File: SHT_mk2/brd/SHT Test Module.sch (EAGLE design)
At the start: 12 parts

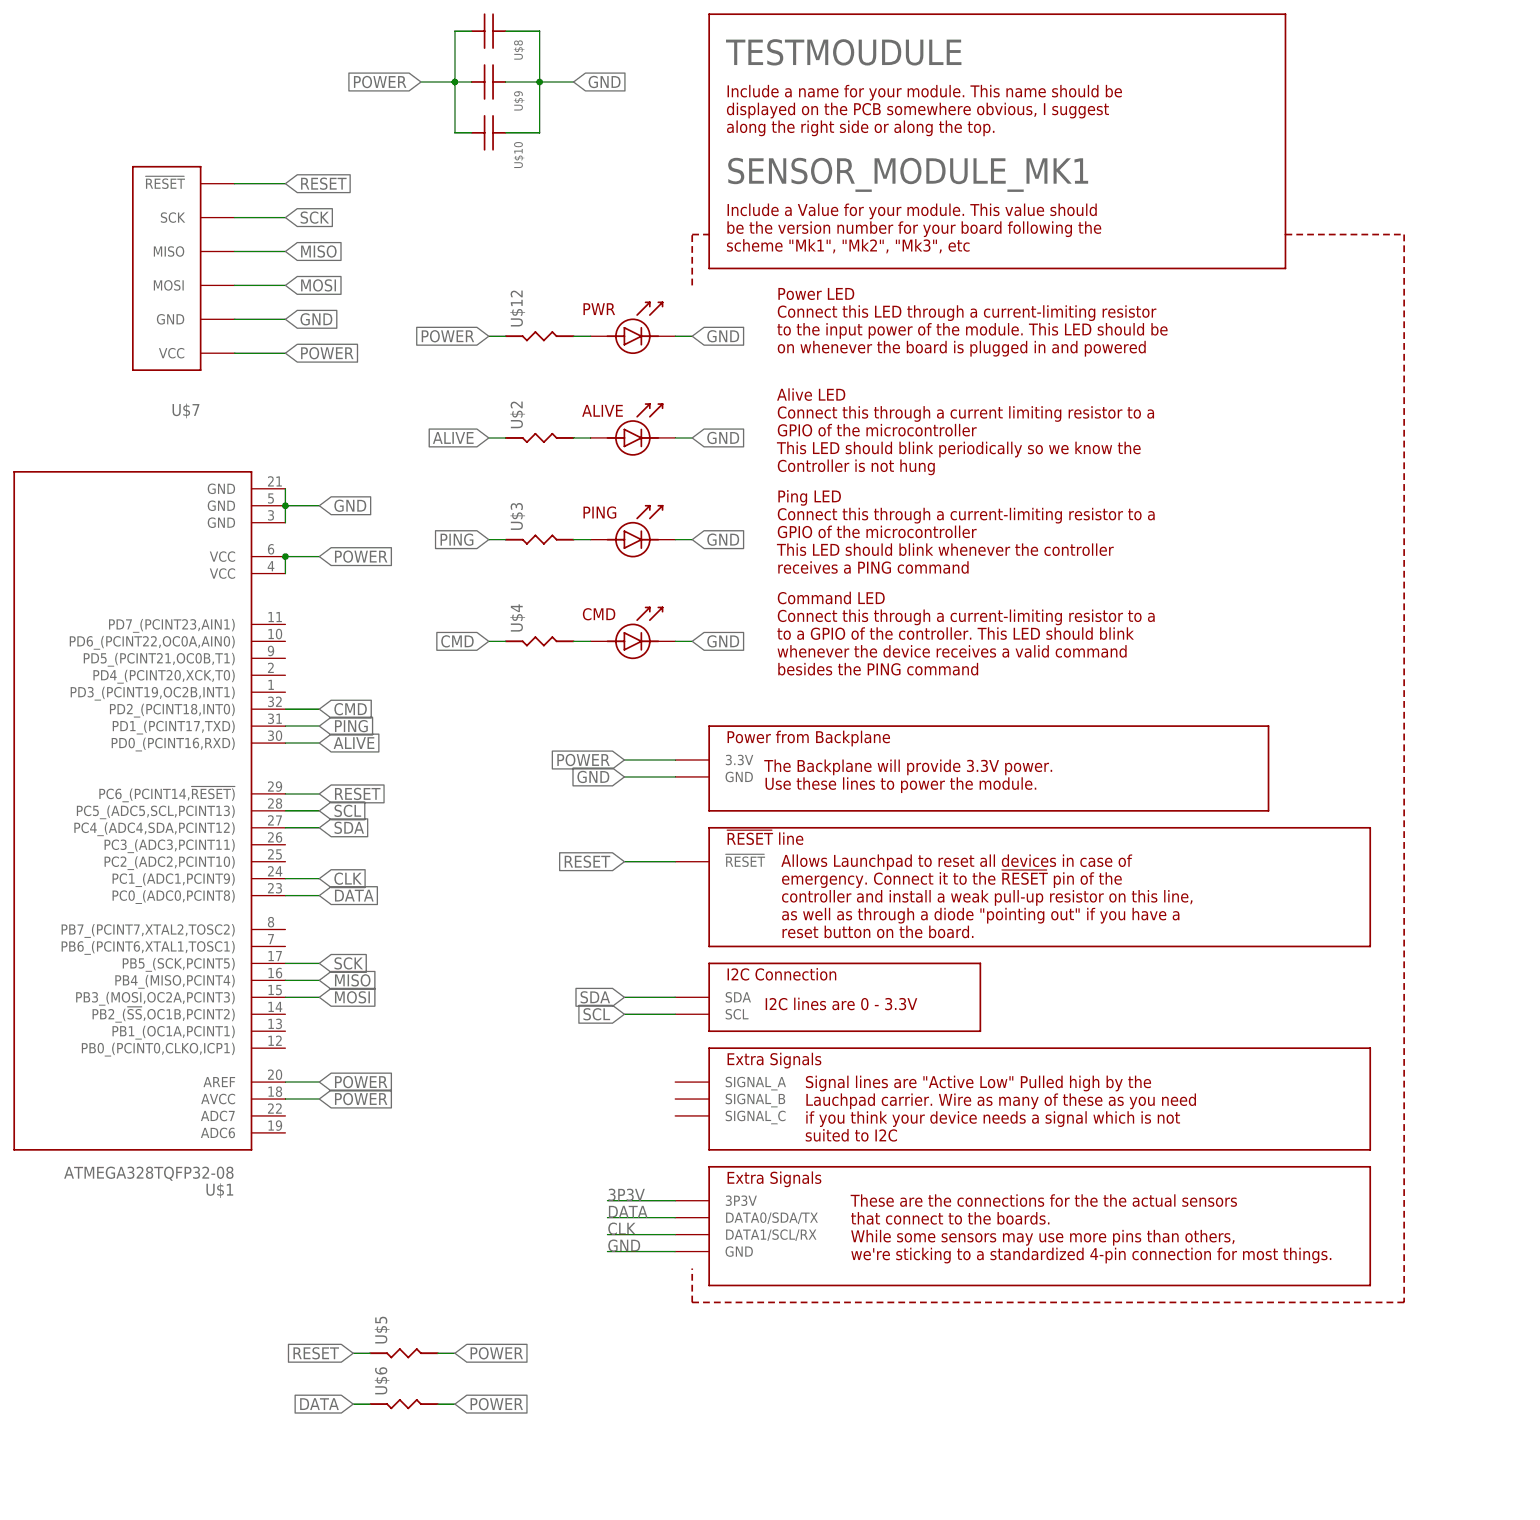
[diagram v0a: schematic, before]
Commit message: pulled over the SHT mk2 brd files from nathan's branch.
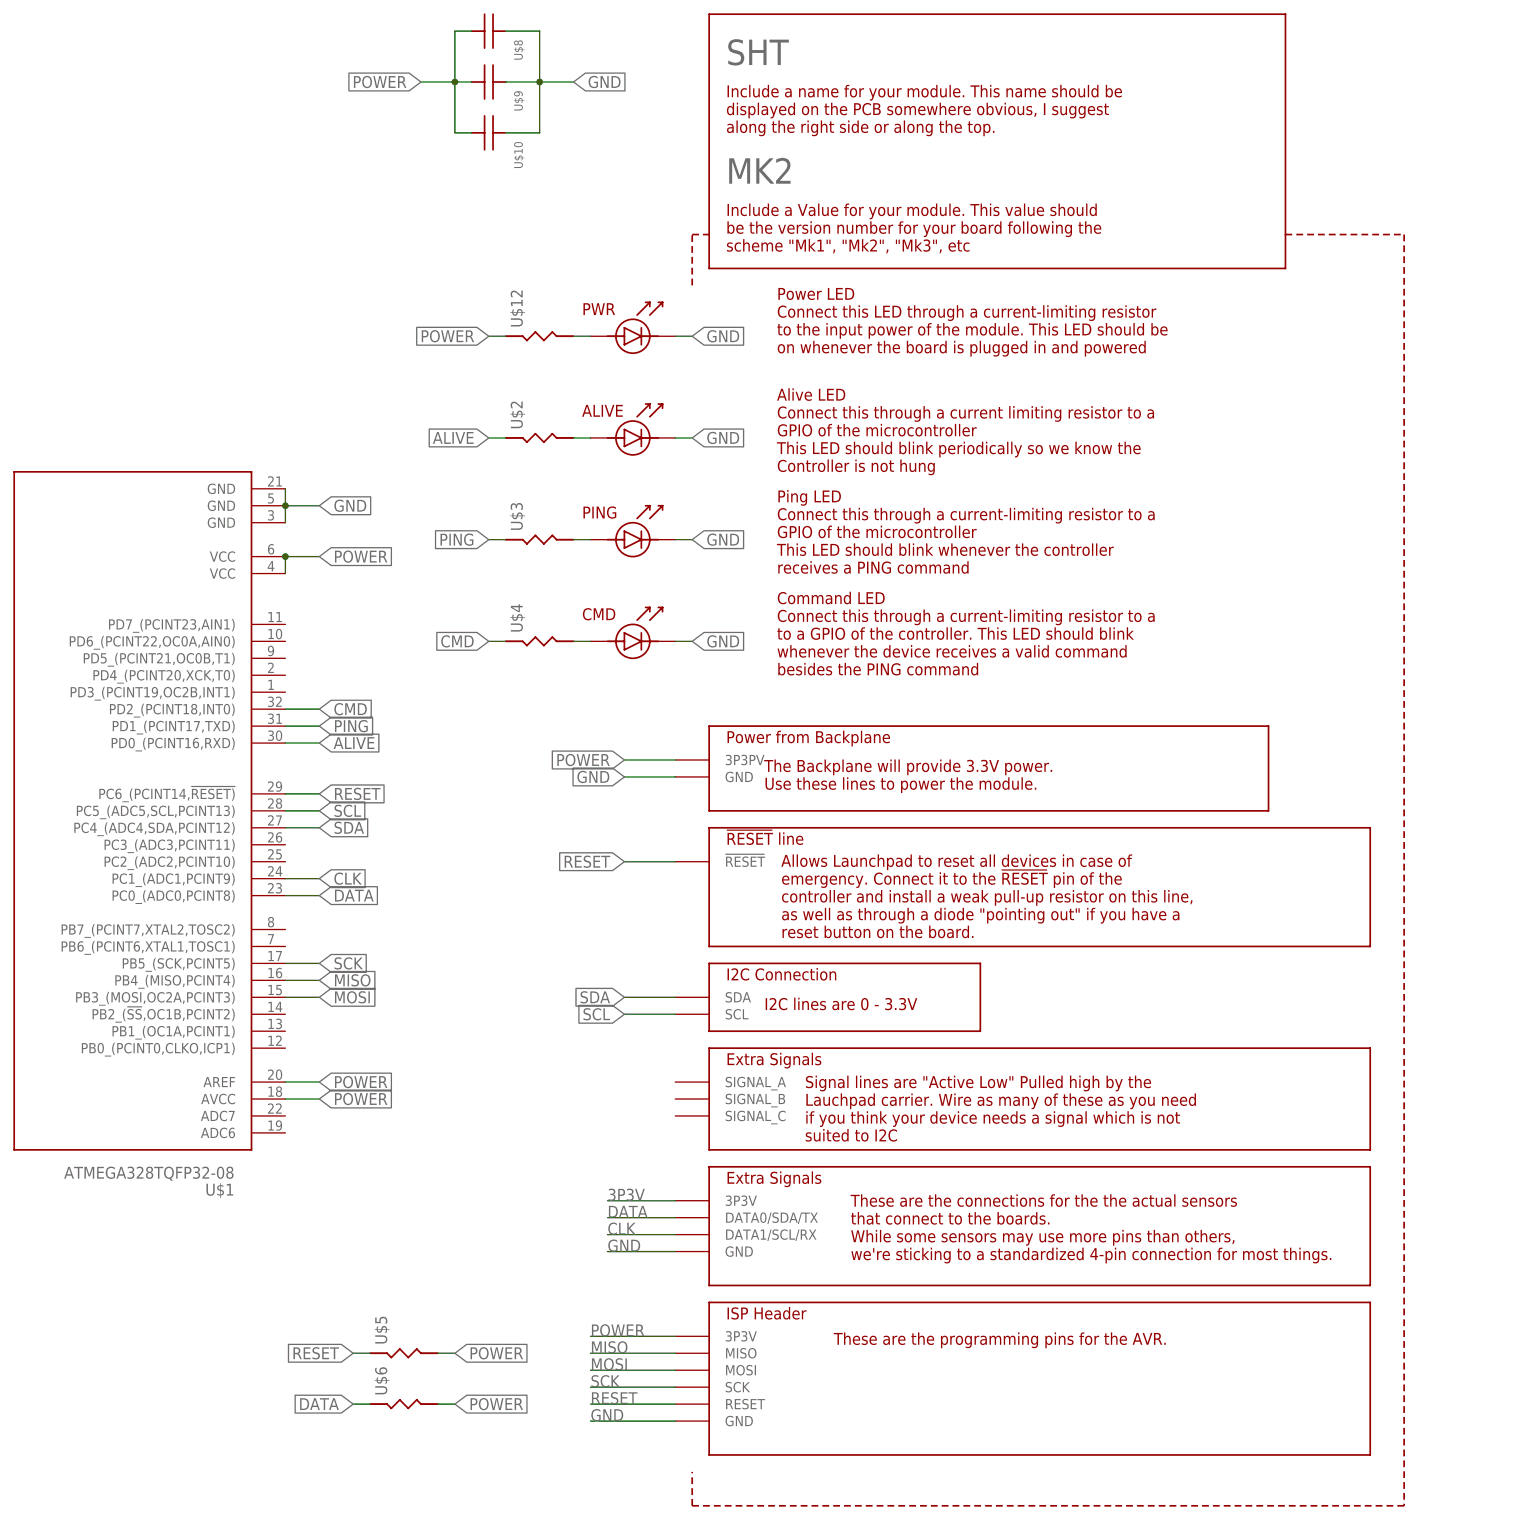
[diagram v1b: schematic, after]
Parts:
- removed U$7: (no value), 000_CustomPartsMaster:ISP_PROGRAMMING_HEADER
- SHT: value SENSOR_MODULE_MK1 -> MK2
- renumbered TESTMOUDULE to SHT
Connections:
- net 3P3V: now also SHT.3P3V@2; no longer SHT.3P3V
- net GND: now also SHT.GND@3; no longer U$7.GND
- net MISO: now also SHT.MISO; no longer U$7.MISO
- net MOSI: now also SHT.MOSI; no longer U$7.MOSI
- net POWER: now also SHT.3P3PV@1, SHT.3P3V@3; no longer SHT.3.3V, U$7.VCC
- net RESET: now also SHT.RESET; no longer U$7.!RESET
- net SCK: now also SHT.SCK; no longer U$7.SCK
